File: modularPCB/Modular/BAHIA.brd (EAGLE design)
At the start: 100 x 80 mm, 3 parts

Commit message: Actualización de pcbs
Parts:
- removed U$2: LCD+I2C, MODULAR:LCD
- removed U$3: RFID, MODULAR:RFID
- added SG2: F/CM12P, buzzer:F/CM12P
- added SV1: (no value), con-lstb:MA04-1
- added SV2: (no value), con-lstb:MA07-1
- moved U$1 25.9 mm to (27.9, 38.1), turned to 90 degrees
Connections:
- removed net N$1: U$1.D21, U$3.SDA
- removed net N$10: U$1.D26, U$2.SCL
- removed net N$11: U$1.D25, U$2.SDA
- removed net N$2: U$1.D18, U$3.SCK
- removed net N$3: U$1.D23, U$3.MOSI
- removed net N$4: U$1.D19, U$3.MISO
- removed net N$5: U$1.GND@1, U$3.GND
- removed net N$6: U$1.D22, U$3.RST
- removed net N$7: U$1.3V3, U$3.3.3V
- removed net N$8: U$1.VIN, U$2.VCC
- removed net N$9: U$1.GND@0, U$2.GND
- new net 3V3: SV2.7, U$1.3V3
- new net BUZZER: SG2.+, U$1.D33
- new net GND: SG2.-, SV1.2, SV2.6, U$1.GND@0, U$1.GND@1
- new net MISO: SV2.4, U$1.D19
- new net MOSI: SV2.1, U$1.D23
- new net RST: SV2.2, U$1.D22
- new net SCK: SV2.5, U$1.D18
- new net SCL: SV1.3, U$1.D26
- new net SDA: SV2.3, U$1.D21
- new net SDA_I2C: SV1.4, U$1.D25
- new net VCC: SV1.1, U$1.VIN
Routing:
- net MOSI: track 0.00 -> 51.6 mm
- net RST: track 0.00 -> 48.0 mm
- net SDA: track 0.00 -> 39.3 mm
- net GND: track 0.00 -> 37.6 mm
- net MISO: track 0.00 -> 35.7 mm
- net SCK: track 0.00 -> 32.1 mm
- net SCL: track 0.00 -> 16.3 mm
- net SDA_I2C: track 0.00 -> 15.5 mm
- net 3V3: track 0.00 -> 11.2 mm
- net BUZZER: track 0.00 -> 11.0 mm
- net VCC: track 0.00 -> 7.62 mm
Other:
- board size 100 x 80 mm -> 43 x 54.5 mm
- board text added: "3v3"
- board text added: "GND"
- board text added: "MISO"
- board text added: "MOSI"
- board text added: "RST"
- board text added: "SCK"
- board text added: "SCL"
- board text added: "SDA"
- board text added: "VCC"

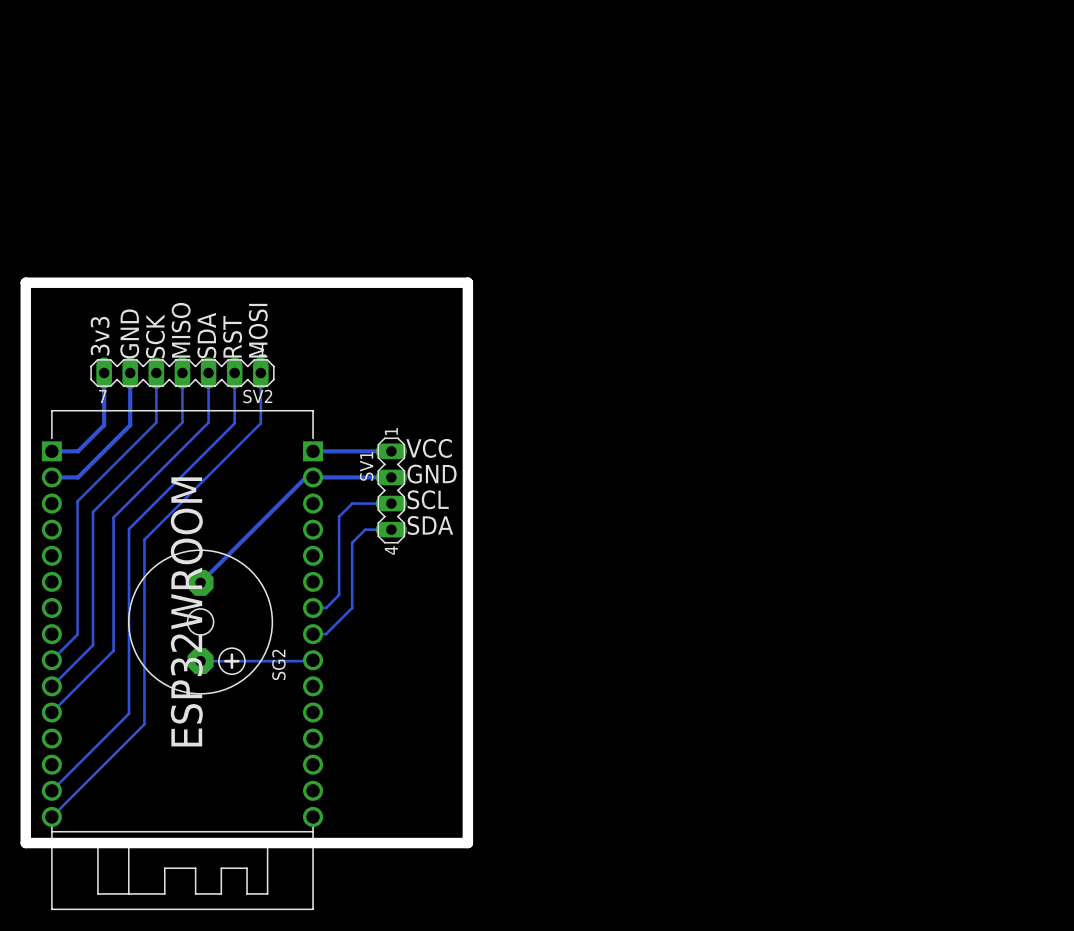
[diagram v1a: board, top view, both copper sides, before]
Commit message: Actualización de PCB de bahía: Pistas y borneras
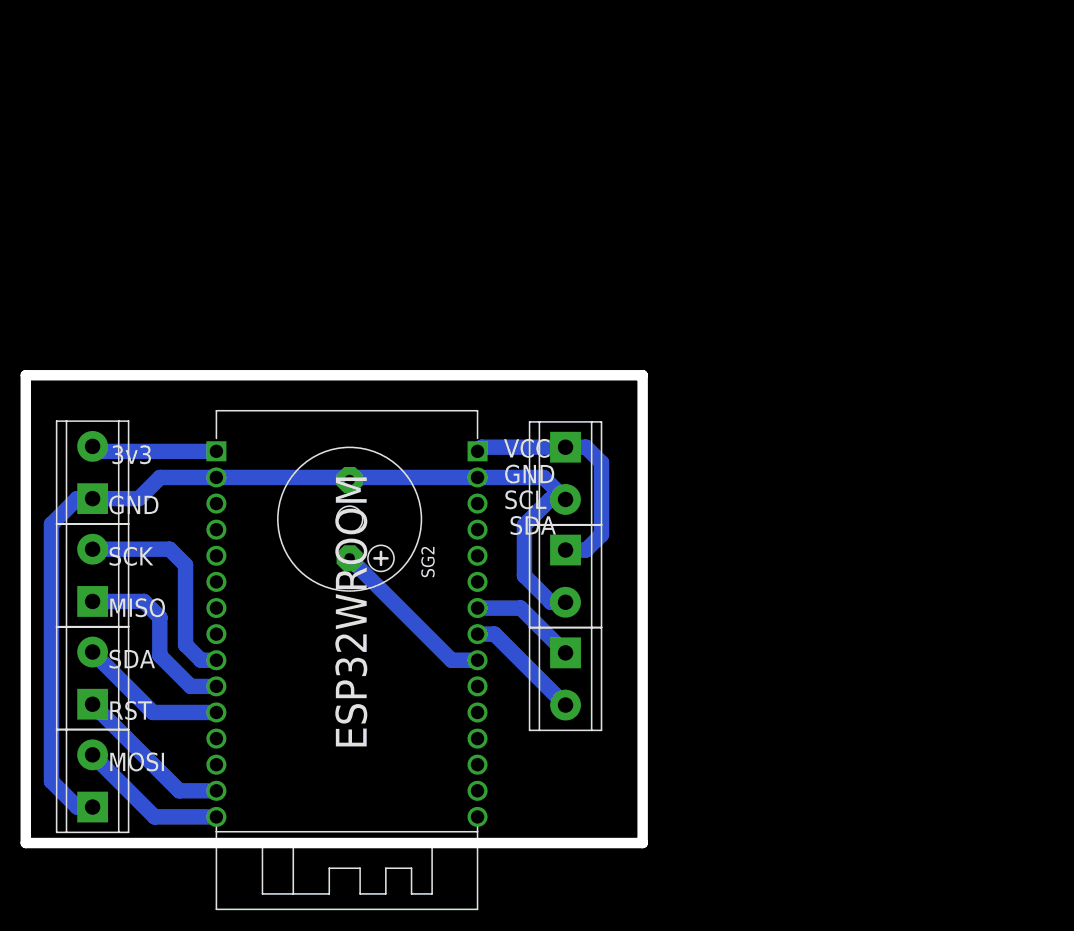
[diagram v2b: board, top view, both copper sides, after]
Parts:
- removed SV1: (no value), con-lstb:MA04-1
- removed SV2: (no value), con-lstb:MA07-1
- added U$2, U$3, U$4, U$5, U$6, U$7, U$8: CLEMAS, MODULAR:CLEMAS
- moved SG2 17.6 mm to (31.5, 31.5)
- moved U$1 16.0 mm to (43.9, 38.1)
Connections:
- net 3V3: now also U$5.2; no longer SV2.7
- net GND: now also U$2.1, U$5.1, U$6.2, U$7.2; no longer SV1.2, SV2.6
- net MISO: now also U$4.1; no longer SV2.4
- net MOSI: now also U$2.2; no longer SV2.1
- net RST: now also U$3.1; no longer SV2.2
- net SCK: now also U$4.2; no longer SV2.5
- net SCL: now also U$8.1; no longer SV1.3
- net SDA: now also U$3.2; no longer SV2.3
- net SDA_I2C: now also U$8.2; no longer SV1.4
- net VCC: now also U$6.1, U$7.1; no longer SV1.1
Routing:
- net GND: track 37.6 -> 98.0 mm
- net MOSI: track 51.6 -> 14.5 mm
- net RST: track 48.0 -> 15.5 mm
- net SDA: track 39.3 -> 14.5 mm
- net MISO: track 35.7 -> 17.6 mm
- net VCC: track 7.62 -> 24.0 mm
- net SCK: track 32.1 -> 21.1 mm
- net SCL: track 16.3 -> 10.4 mm
- net BUZZER: track 11.0 -> 16.5 mm
- net SDA_I2C: track 15.5 -> 11.4 mm
- net 3V3: track 11.2 -> 12.2 mm
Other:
- board size 43 x 54.5 mm -> 60 x 45.5 mm
